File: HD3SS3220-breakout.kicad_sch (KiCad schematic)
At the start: 0 parts

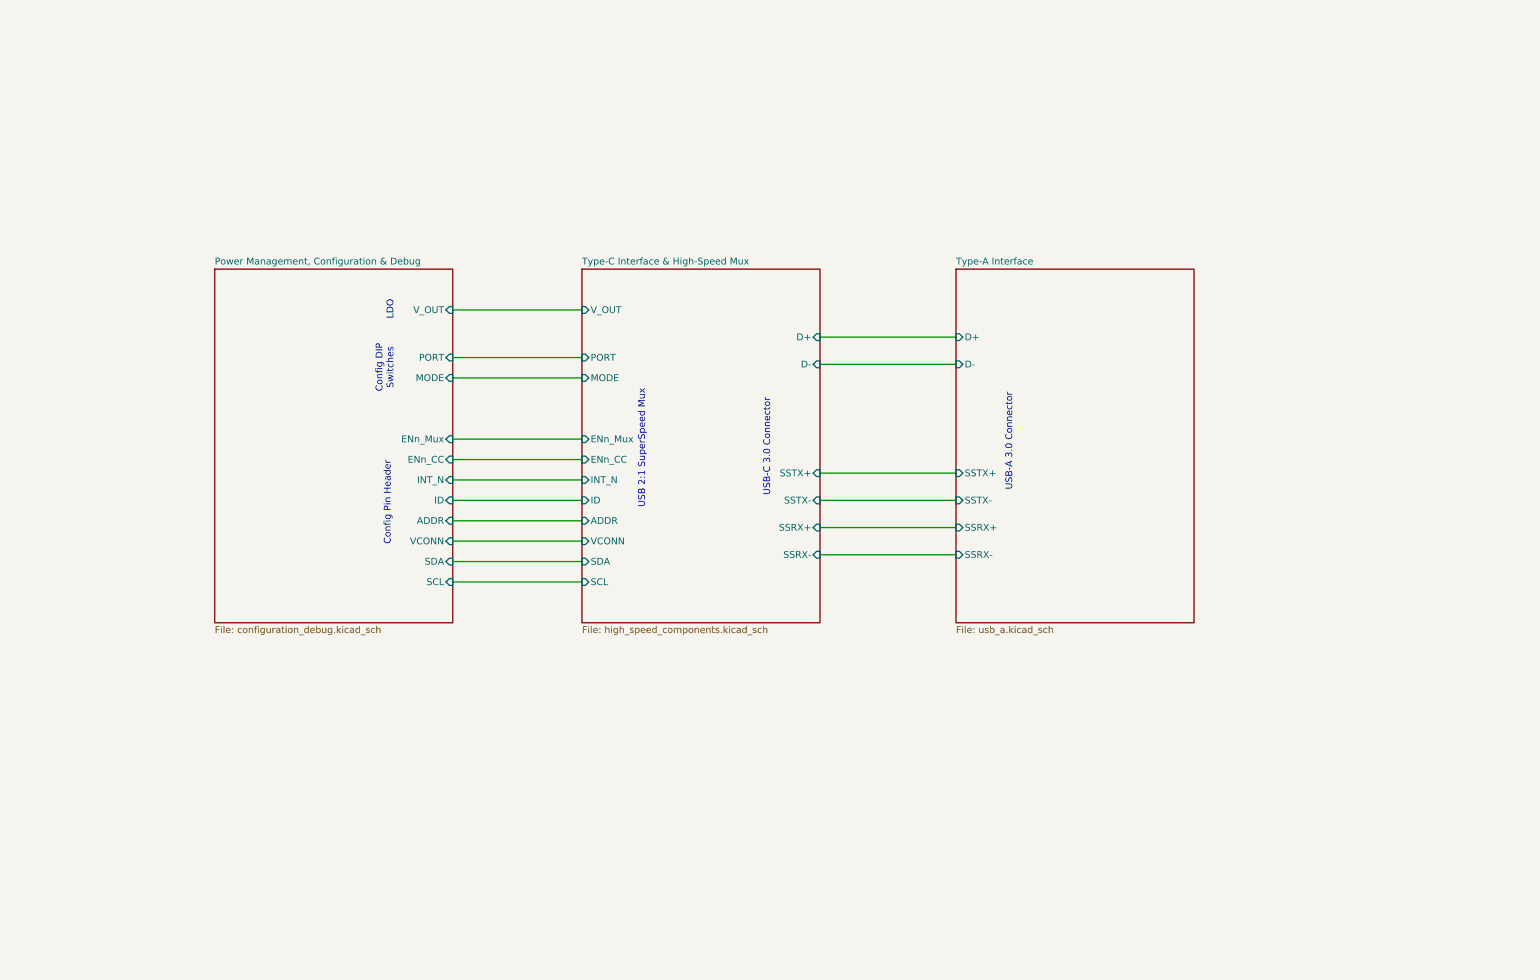
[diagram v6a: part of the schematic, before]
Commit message: Added missing components (Coupling capacitors and led resistors, wired board again
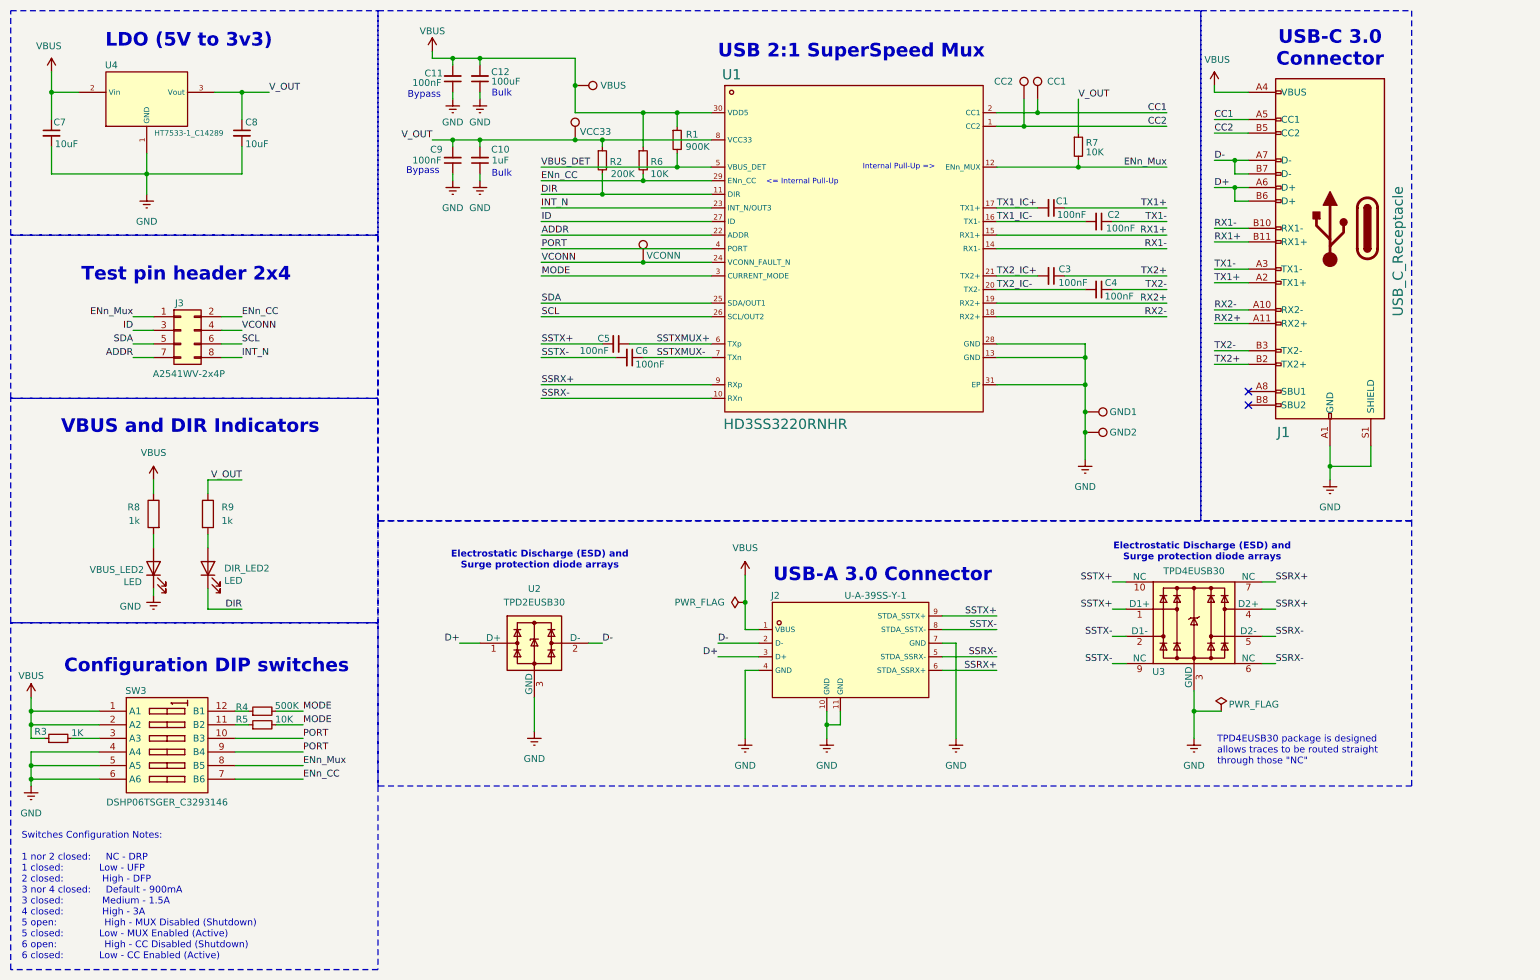
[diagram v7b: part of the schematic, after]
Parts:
- added C1, C11, C2, C3, C4, C5, C6, C9: 100nF, Capacitor_SMD:C_0402_1005Metric, symbol Device:C_Small
- added C10: 1uF, Capacitor_SMD:C_0402_1005Metric, symbol Device:C_Small
- added C12: 100uF, Capacitor_SMD:C_0402_1005Metric, symbol Device:C_Small
- added C7, C8: 10uF, Capacitor_SMD:C_0402_1005Metric, symbol Device:C_Small
- added DIR_LED2, VBUS_LED2: LED, LED_SMD:LED_0603_1608Metric, symbol Device:LED
- added J1: USB_C_Receptacle, Interface_USB:USB-C-SMD_TYPE-C-USB-19, symbol Connector:USB_C_Receptacle
- added J2: U-A-39SS-Y-1, Interface_USB:USB-3.0-A_U-A-39SS-Y-1, symbol Connector_USB-custom:U-A-39SS-Y-1
- added J3: A2541WV-2x4P, Connector_PinHeader_2.54mm:PinHeader_2x04_P2.54mm_Vertical, symbol Connector_Generic:Conn_02x04_Odd_Even
- added R1: 900K, Resistor_SMD:R_0805_2012Metric, symbol Device:R_Small
- added R2: 200K, Resistor_SMD:R_0402_1005Metric, symbol Device:R_Small
- added R3: 1K, Resistor_SMD:R_0402_1005Metric, symbol Device:R_Small
- added R4: 500K, Resistor_SMD:R_0805_2012Metric, symbol Device:R_Small
- added R5, R6, R7: 10K, Resistor_SMD:R_0402_1005Metric, symbol Device:R_Small
- added R8, R9: 1k, Resistor_SMD:R_0402_1005Metric, symbol Device:R
- added SW3: DSHP06TSGER_C3293146, UWReality_Labs:SW-SMD_12P-L9.2-W5.4-P1.27-LS8.5, symbol UWRealityLabs:DSHP06TSGER_C3293146
- added TP1: VBUS, TestPoint:TestPoint_Pad_D1.5mm, symbol Connector:TestPoint
- added TP2: VCONN, TestPoint:TestPoint_Pad_D1.5mm, symbol Connector:TestPoint
- added TP3: VCC33, TestPoint:TestPoint_Pad_D1.5mm, symbol Connector:TestPoint
- added TP4: GND1, TestPoint:TestPoint_Keystone_5000-5004_Miniature, symbol Connector:TestPoint
- added TP5: GND2, TestPoint:TestPoint_Keystone_5000-5004_Miniature, symbol Connector:TestPoint
- added TP6: CC2, TestPoint:TestPoint_Pad_D1.5mm, symbol Connector:TestPoint
- added TP7: CC1, TestPoint:TestPoint_Pad_D1.5mm, symbol Connector:TestPoint
- added U1: HD3SS3220RNHR, Interface_USB:HD3SS3220IRNHR, symbol Interface_USB:HD3SS3220RNHR
- added U2: TPD2EUSB30, Package_TO_SOT_SMD:Texas_DRT-3, symbol Power_Protection:TPD2EUSB30
- added U3: TPD4EUSB30, Package_SON:USON-10_2.5x1.0mm_P0.5mm, symbol Power_Protection:TPD4EUSB30
- added U4: HT7533-1_C14289, Interface_USB:SOT-89-3_L4.5-W2.5-P1.50-LS4.2-BR, symbol Regulator_Linear:HT7533-1_C14289
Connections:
- new net: C10.2, C8.1, C9.2, R2.1, R7.1, R9.1, TP3.1, U1.8 (VCC33), U4.3 (Vout)
- new net: DIR_LED2.2 (A), R9.2
- new net: R5.1, SW3.11 (B2)
- new net: R4.1, SW3.12 (B1)
- new net: R3.2, SW3.3 (A3)
- new net: R8.2, VBUS_LED2.2 (A)
- new net ADDR: J3.7 (Pin_7), U1.22 (ADDR)
- new net CC1: J1.A5 (CC1), TP7.1, U1.2 (CC1)
- new net CC2: J1.B5 (CC2), TP6.1, U1.1 (CC2)
- new net D+: J1.A6 (D+), J1.B6 (D+), J2.3 (D+), U2.1 (D+)
- new net D-: J1.A7 (D-), J1.B7 (D-), J2.2 (D-), U2.2 (D-)
- new net DIR: DIR_LED2.1 (K), R2.2, U1.11 (DIR)
- new net ENn_CC: J3.2 (Pin_2), R6.2, SW3.7 (B6), U1.29 (ENn_CC)
- new net ENn_Mux: J3.1 (Pin_1), R7.2, SW3.8 (B5), U1.12 (ENn_MUX)
- new net GND: C10.1, C11.1, C12.1, C7.2, C8.2, C9.1, J1.A1 (GND), J1.A12 (GND), J1.B1 (GND), J1.B12 (GND), J1.S1 (SHIELD), J2.10 (GND), J2.11 (GND), J2.4 (GND), J2.7 (GND), SW3.4 (A4), SW3.5 (A5), SW3.6 (A6), TP4.1, TP5.1, U1.13 (GND), U1.28 (GND), U1.31 (EP), U2.3 (GND), U3.3 (GND), U3.8 (GND), U4.1 (GND), VBUS_LED2.1 (K)
- new net ID: J3.3 (Pin_3), U1.27 (ID)
- new net INT_N: J3.8 (Pin_8), U1.23 (INT_N/OUT3)
- new net MODE: R4.2, R5.2, U1.3 (CURRENT_MODE)
- new net PORT: SW3.10 (B3), SW3.9 (B4), U1.4 (PORT)
- new net RX1+: J1.B11 (RX1+), U1.15 (RX1+)
- new net RX1-: J1.B10 (RX1-), U1.14 (RX1-)
- new net RX2+: J1.A11 (RX2+), U1.19 (RX2+)
- new net RX2-: J1.A10 (RX2-), U1.18 (RX2+)
- new net SCL: J3.6 (Pin_6), U1.26 (SCL/OUT2)
- new net SDA: J3.5 (Pin_5), U1.25 (SDA/OUT1)
- new net SSRX+: J2.6 (STDA_SSRX+), U1.9 (RXp), U3.4 (D2+), U3.7 (NC)
- new net SSRX-: J2.5 (STDA_SSRX-), U1.10 (RXn), U3.5 (D2-), U3.6 (NC)
- new net SSTX+: C5.2, J2.9 (STDA_SSTX+), U3.1 (D1+), U3.10 (NC)
- new net SSTX-: C6.2, J2.8 (STDA_SSTX-), U3.2 (D1-), U3.9 (NC)
- new net SSTXMUX+: C5.1, U1.6 (TXp)
- new net SSTXMUX-: C6.1, U1.7 (TXn)
- new net TX1+: C1.1, J1.A2 (TX1+)
- new net TX1-: C2.1, J1.A3 (TX1-)
- new net TX1_IC+: C1.2, U1.17 (TX1+)
- new net TX1_IC-: C2.2, U1.16 (TX1-)
- new net TX2+: C3.1, J1.B2 (TX2+)
- new net TX2-: C4.1, J1.B3 (TX2-)
- new net TX2_IC+: C3.2, U1.21 (TX2+)
- new net TX2_IC-: C4.2, U1.20 (TX2-)
- new net VBUS: C11.2, C12.2, C7.1, J1.A4 (VBUS), J1.A9 (VBUS), J1.B4 (VBUS), J1.B9 (VBUS), J2.1 (VBUS), R1.1, R3.1, R6.1, R8.1, SW3.1 (A1), SW3.2 (A2), TP1.1, U1.30 (VDD5), U4.2 (Vin)
- new net VBUS_DET: R1.2, U1.5 (VBUS_DET)
- new net VCONN: J3.4 (Pin_4), TP2.1, U1.24 (VCONN_FAULT_N)
- no-connect marks 0 -> 2
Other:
- removed sheet Power Management, Configuration & Debug
- removed sheet Type-A Interface
- removed sheet Type-C Interface & High-Speed Mux
- note added: "<= Internal Pull-Up"
- note added: "Bulk"
- note added: "Bypass"
- note added: "Configuration DIP switches"
- note added: "Electrostatic Discharge (ESD) and Surge protection diode arrays"
- note added: "Internal Pull-Up =>"
- note added: "LDO (5V to 3v3)"
- note added: "Switches Configuration Notes: 1 nor 2 closed: NC - DRP 1 closed: Low - UFP 2 closed: High - DFP 3 nor 4 closed: Default - 900mA 3 closed: Medium - 1.5A 4 closed: High - 3A 5 open: High - MUX Disabled (Shutdown) 5 closed: Low - MUX Enabled (Active) 6 open: High - CC Disabled (Shutdown) 6 closed: Low - CC Enabled (Active)"
- note added: "TPD4EUSB30 package is designed allows traces to be routed straight through those "NC""
- note added: "Test pin header 2x4"
- note added: "VBUS and DIR Indicators"
- note removed: "Config DIP Switches"
- note removed: "Config Pin Header"
- note removed: "LDO"

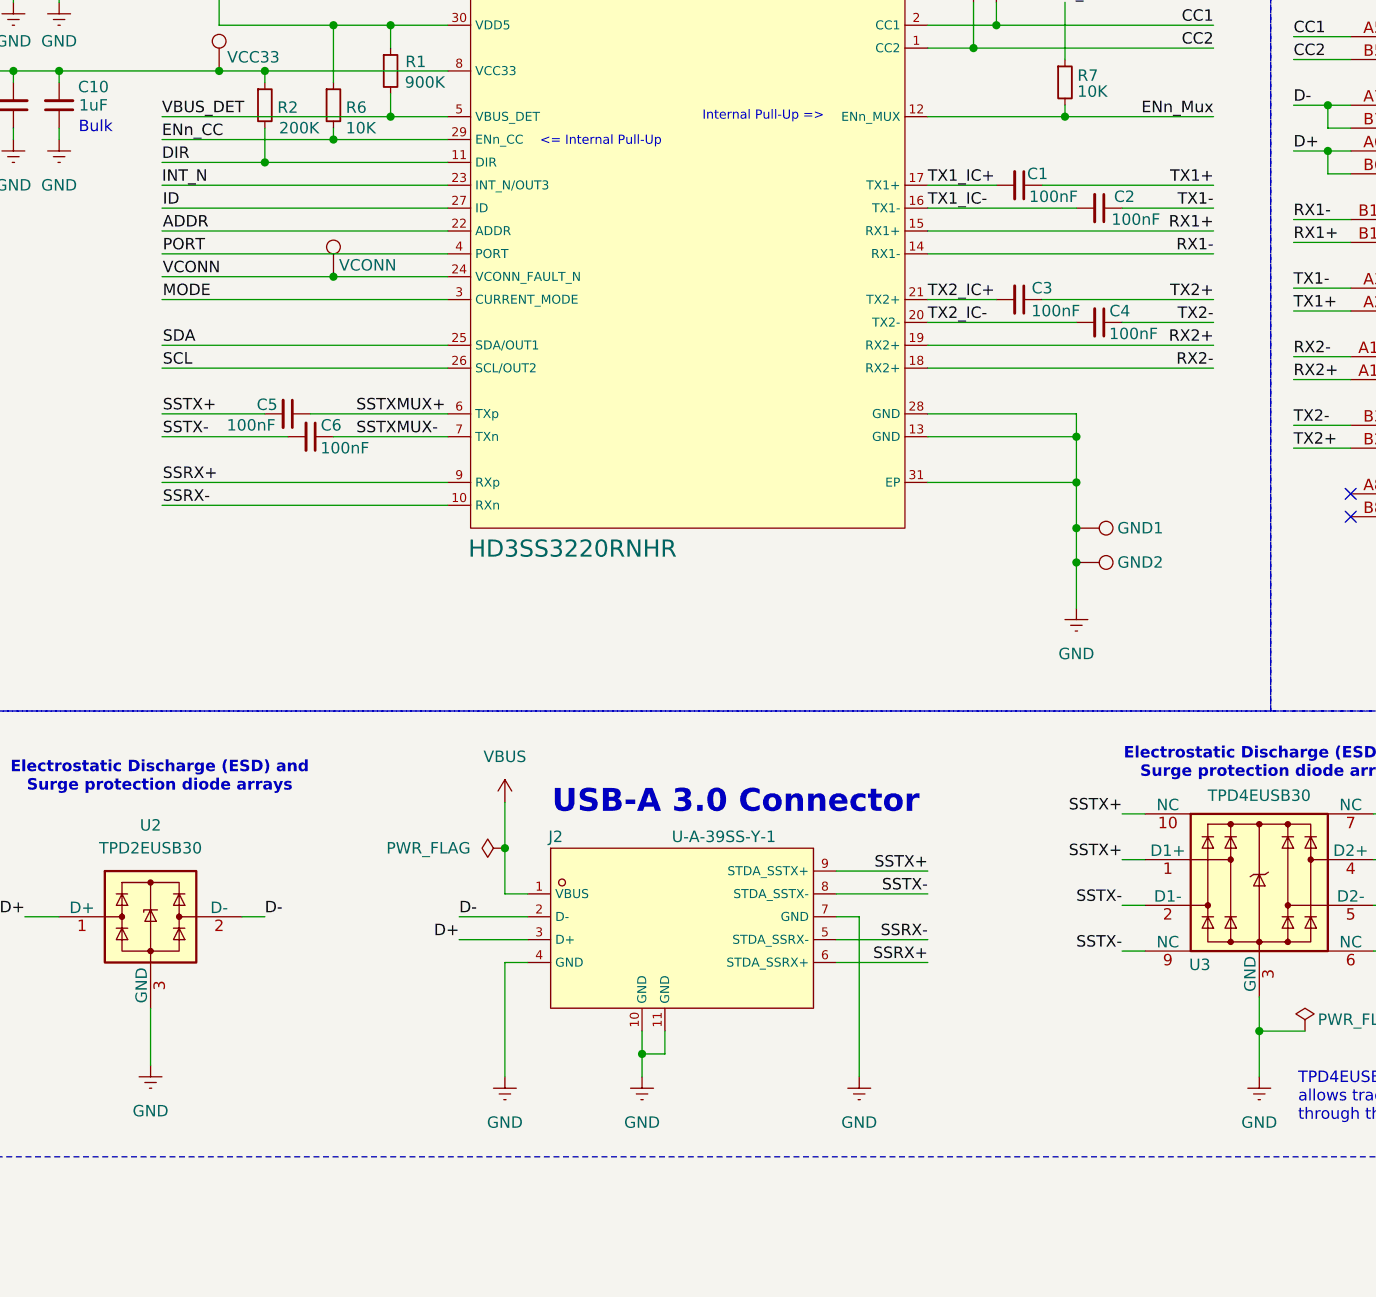
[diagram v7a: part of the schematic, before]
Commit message: Schematic Review: Removed Coupling Capacitors (no USB controller just mux)
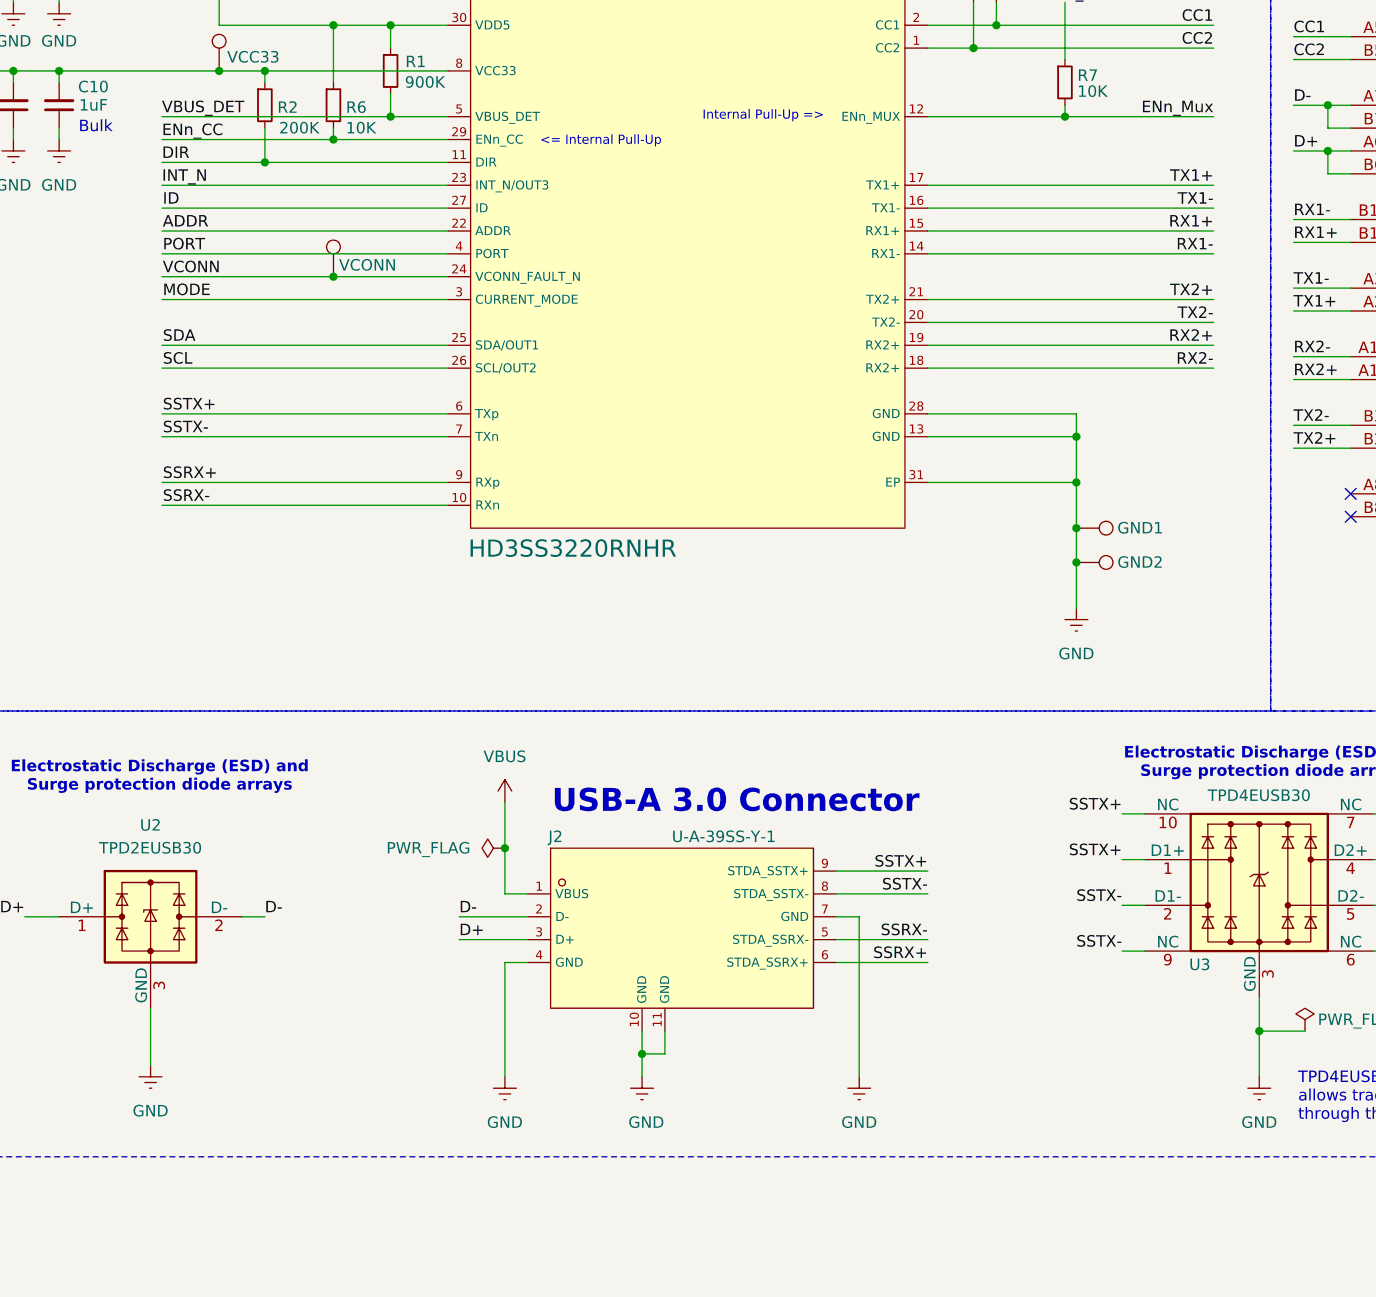
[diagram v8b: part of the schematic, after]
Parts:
- removed C1, C2, C3, C4, C5, C6: 100nF, Capacitor_SMD:C_0402_1005Metric, symbol Device:C_Small
- C12: footprint Capacitor_SMD:C_0402_1005Metric -> Capacitor_SMD:C_1210_3225Metric; LCSC C106204 -> C394395; Store Page https://www.lcsc.com/product-detail/C106204.html -> https://www.lcsc.com/product-detail/C394395.html
- J1: LCSC C2765186 -> C2927039; Store Page https://www.lcsc.com/product-detail/C22359725.html -> https://www.lcsc.com/product-detail/C2927039.html
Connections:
- net SSTXMUX+ is gone; now on net SSTX+: U1.6 (TXp)
- net SSTXMUX- is gone; now on net SSTX-: U1.7 (TXn)
- net TX1_IC+ is gone; now on net TX1+: U1.17 (TX1+)
- net TX1_IC- is gone; now on net TX1-: U1.16 (TX1-)
- net TX2_IC+ is gone; now on net TX2+: U1.21 (TX2+)
- net TX2_IC- is gone; now on net TX2-: U1.20 (TX2-)
